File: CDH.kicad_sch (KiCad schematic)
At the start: 45 parts, among them J3 G125-MH12605M4P, J4 Conn_ARM_JTAG_SWD_10, U1 STM32H745BITx, U2 MCP2562FDT-H_SN

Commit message: PCB
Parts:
- C1, C10, C11, C12, C13, C14, C15, C16, C17, C18, C2, C21, C26, C27, C3, C4, C5, C6, C7, C8, C9: footprint (none) -> Capacitor_SMD:C_0402_1005Metric
- C19, C22, C23, C24, C28: footprint (none) -> Capacitor_SMD:C_0805_2012Metric
- C20: footprint (none) -> Capacitor_SMD:C_0603_1608Metric
- C25: value C -> 100n; footprint (none) -> Capacitor_SMD:C_0402_1005Metric
- FB1: footprint (none) -> Inductor_SMD:L_0201_0603Metric
- J4: footprint (none) -> Connector_PinHeader_1.27mm:PinHeader_2x05_P1.27mm_Horizontal
- JP1: footprint (none) -> Jumper:SolderJumper-2_P1.3mm_Bridged2Bar_Pad1.0x1.5mm
- JP2: footprint (none) -> Jumper:SolderJumper-2_P1.3mm_Open_Pad1.0x1.5mm
- PC104_H1, PC104_H2: footprint (none) -> Connector_PinHeader_1.00mm:PinHeader_2x26_P1.00mm_Vertical
- R1, R2, R3, R4, R5, R6, R8: footprint (none) -> Resistor_SMD:R_0603_1608Metric
- SW_Reset1: footprint (none) -> Button_Switch_SMD:SW_Push_1P1T-SH_NO_CK_KMR2xxG
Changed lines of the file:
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@@
 			)
 		)
-		(property "Footprint" ""
+		(property "Footprint" "Capacitor_SMD:C_0402_1005Metric"
 			(at 268.9352 34.29 0)
 			(effects
@@
 			)
 		)
-		(property "Value" "C"
+		(property "Value" "100n"
 			(at 247.904 82.55 90)
 			(effects
@@
 			)
 		)
-		(property "Footprint" ""
+		(property "Footprint" "Capacitor_SMD:C_0402_1005Metric"
 			(at 241.3 79.7052 0)
 			(effects
@@
 			)
 		)
-		(property "Footprint" ""
+		(property "Footprint" "Resistor_SMD:R_0603_1608Metric"
 			(at 450.342 236.22 90)
 			(effects
@@
 			)
 		)
-		(property "Footprint" ""
+		(property "Footprint" "Capacitor_SMD:C_0603_1608Metric"
 			(at 346.4052 55.88 0)
 			(effects
@@
 			)
 		)
-		(property "Footprint" ""
+		(property "Footprint" "Capacitor_SMD:C_0805_2012Metric"
 			(at 341.63 75.2348 0)
 			(effects
@@
 			)
 		)
-		(property "Footprint" ""
+		(property "Footprint" "Capacitor_SMD:C_0402_1005Metric"
 			(at 277.8252 34.29 0)
 			(effects
@@
 			)
 		)
-		(property "Footprint" ""
+		(property "Footprint" "Capacitor_SMD:C_0402_1005Metric"
 			(at 286.7152 55.88 0)
 			(effects
@@
 			)
 		)
-		(property "Footprint" ""
+		(property "Footprint" "Resistor_SMD:R_0603_1608Metric"
 			(at 239.522 270.51 90)
 			(effects
@@
 			)
 		)
-		(property "Footprint" ""
+		(property "Footprint" "Capacitor_SMD:C_0402_1005Metric"
 			(at 322.2752 55.88 0)
 			(effects
@@
 			)
 		)
-		(property "Footprint" ""
+		(property "Footprint" "Capacitor_SMD:C_0402_1005Metric"
 			(at 295.6052 34.29 0)
 			(effects
@@
 			)
 		)
-		(property "Footprint" ""
+		(property "Footprint" "Capacitor_SMD:C_0805_2012Metric"
 			(at 247.65 316.5348 0)
 			(effects
@@
 			)
 		)
-		(property "Footprint" ""
+		(property "Footprint" "Resistor_SMD:R_0603_1608Metric"
 			(at 239.522 260.35 90)
 			(effects
@@
 			)
 		)
-		(property "Footprint" ""
+		(property "Footprint" "Resistor_SMD:R_0603_1608Metric"
 			(at 367.792 153.67 90)
 			(effects
@@
 			)
 		)
-		(property "Footprint" ""
+		(property "Footprint" "Capacitor_SMD:C_0402_1005Metric"
 			(at 313.3852 34.29 0)
 			(effects
@@
 			)
 		)
-		(property "Footprint" ""
+		(property "Footprint" "Capacitor_SMD:C_0402_1005Metric"
 			(at 331.1652 34.29 0)
 			(effects
@@
 			)
 		)
-		(property "Footprint" ""
+		(property "Footprint" "Capacitor_SMD:C_0402_1005Metric"
 			(at 357.8352 55.88 0)
 			(effects
@@
 			)
 		)
-		(property "Footprint" ""
+		(property "Footprint" "Capacitor_SMD:C_0402_1005Metric"
 			(at 176.53 129.8448 0)
 			(effects
@@
 			)
 		)
-		(property "Footprint" ""
+		(property "Footprint" "Capacitor_SMD:C_0805_2012Metric"
 			(at 247.65 300.0248 0)
 			(effects
@@
 			)
 		)
-		(property "Footprint" ""
+		(property "Footprint" "Capacitor_SMD:C_0402_1005Metric"
 			(at 304.4952 34.29 0)
 			(effects
@@
 			)
 		)
-		(property "Footprint" ""
+		(property "Footprint" "Capacitor_SMD:C_0402_1005Metric"
 			(at 175.26 142.5448 0)
 			(effects
@@
 			)
 		)
-		(property "Footprint" ""
+		(property "Footprint" "Capacitor_SMD:C_0402_1005Metric"
 			(at 331.1652 55.88 0)
 			(effects
@@
 			)
 		)
-		(property "Footprint" ""
+		(property "Footprint" "Connector_PinHeader_1.00mm:PinHeader_2x26_P1.00mm_Vertical"
 			(at 416.56 144.78 0)
 			(effects
@@
 			)
 		)
-		(property "Footprint" ""
+		(property "Footprint" "Inductor_SMD:L_0201_0603Metric"
 			(at 288.29 66.548 90)
 			(effects
@@
 			)
 		)
-		(property "Footprint" ""
+		(property "Footprint" "Capacitor_SMD:C_0805_2012Metric"
 			(at 247.65 308.9148 0)
 			(effects
@@
 			)
 		)
-		(property "Footprint" ""
+		(property "Footprint" "Resistor_SMD:R_0603_1608Metric"
 			(at 371.348 143.51 90)
 			(effects
@@
 			)
 		)
-		(property "Footprint" ""
+		(property "Footprint" "Capacitor_SMD:C_0805_2012Metric"
 			(at 342.5952 34.29 0)
 			(effects
@@
 			)
 		)
-		(property "Footprint" ""
+		(property "Footprint" "Capacitor_SMD:C_0402_1005Metric"
 			(at 286.7152 34.29 0)
 			(effects
@@
 			)
 		)
-		(property "Footprint" ""
+		(property "Footprint" "Capacitor_SMD:C_0402_1005Metric"
 			(at 277.8252 55.88 0)
 			(effects
@@
 			)
 		)
-		(property "Footprint" ""
+		(property "Footprint" "Capacitor_SMD:C_0402_1005Metric"
 			(at 313.3852 55.88 0)
 			(effects
@@
 			)
 		)
-		(property "Footprint" ""
+		(property "Footprint" "Capacitor_SMD:C_0402_1005Metric"
 			(at 304.4952 55.88 0)
 			(effects
@@
 			)
 		)
-		(property "Footprint" ""
+		(property "Footprint" "Connector_PinHeader_1.00mm:PinHeader_2x26_P1.00mm_Vertical"
 			(at 445.77 144.78 0)
 			(effects
@@
 			)
 		)
-		(property "Footprint" ""
+		(property "Footprint" "Button_Switch_SMD:SW_Push_1P1T-SH_NO_CK_KMR2xxG"
 			(at 245.11 68.58 0)
 			(effects
@@
 			)
 		)
-		(property "Footprint" ""
+		(property "Footprint" "Connector_PinHeader_1.27mm:PinHeader_2x05_P1.27mm_Horizontal"
 			(at 434.34 247.65 0)
 			(effects
@@
 			)
 		)
-		(property "Footprint" ""
+		(property "Footprint" "Jumper:SolderJumper-2_P1.3mm_Bridged2Bar_Pad1.0x1.5mm"
 			(at 246.38 93.98 0)
 			(effects
@@
 			)
 		)
-		(property "Footprint" ""
+		(property "Footprint" "Resistor_SMD:R_0603_1608Metric"
 			(at 116.332 149.86 90)
 			(effects
@@
 			)
 		)
-		(property "Footprint" ""
+		(property "Footprint" "Jumper:SolderJumper-2_P1.3mm_Open_Pad1.0x1.5mm"
 			(at 118.11 139.7 0)
 			(effects
@@
 			)
 		)
-		(property "Footprint" ""
+		(property "Footprint" "Capacitor_SMD:C_0402_1005Metric"
 			(at 268.9352 55.88 0)
 			(effects
@@
 			)
 		)
-		(property "Footprint" ""
+		(property "Footprint" "Capacitor_SMD:C_0402_1005Metric"
 			(at 322.2752 34.29 0)
 			(effects
@@
 			)
 		)
-		(property "Footprint" ""
+		(property "Footprint" "Capacitor_SMD:C_0402_1005Metric"
 			(at 295.6052 55.88 0)
 			(effects
@@
 			)
 		)
-		(property "Footprint" ""
+		(property "Footprint" "Resistor_SMD:R_0603_1608Metric"
 			(at 238.76 90.678 90)
 			(effects
@@
 			)
 		)
-		(property "Footprint" ""
+		(property "Footprint" "Capacitor_SMD:C_0402_1005Metric"
 			(at 260.0452 34.29 0)
 			(effects
@@
 			)
 		)
-		(property "Footprint" ""
+		(property "Footprint" "Capacitor_SMD:C_0402_1005Metric"
 			(at 260.0452 55.88 0)
 			(effects

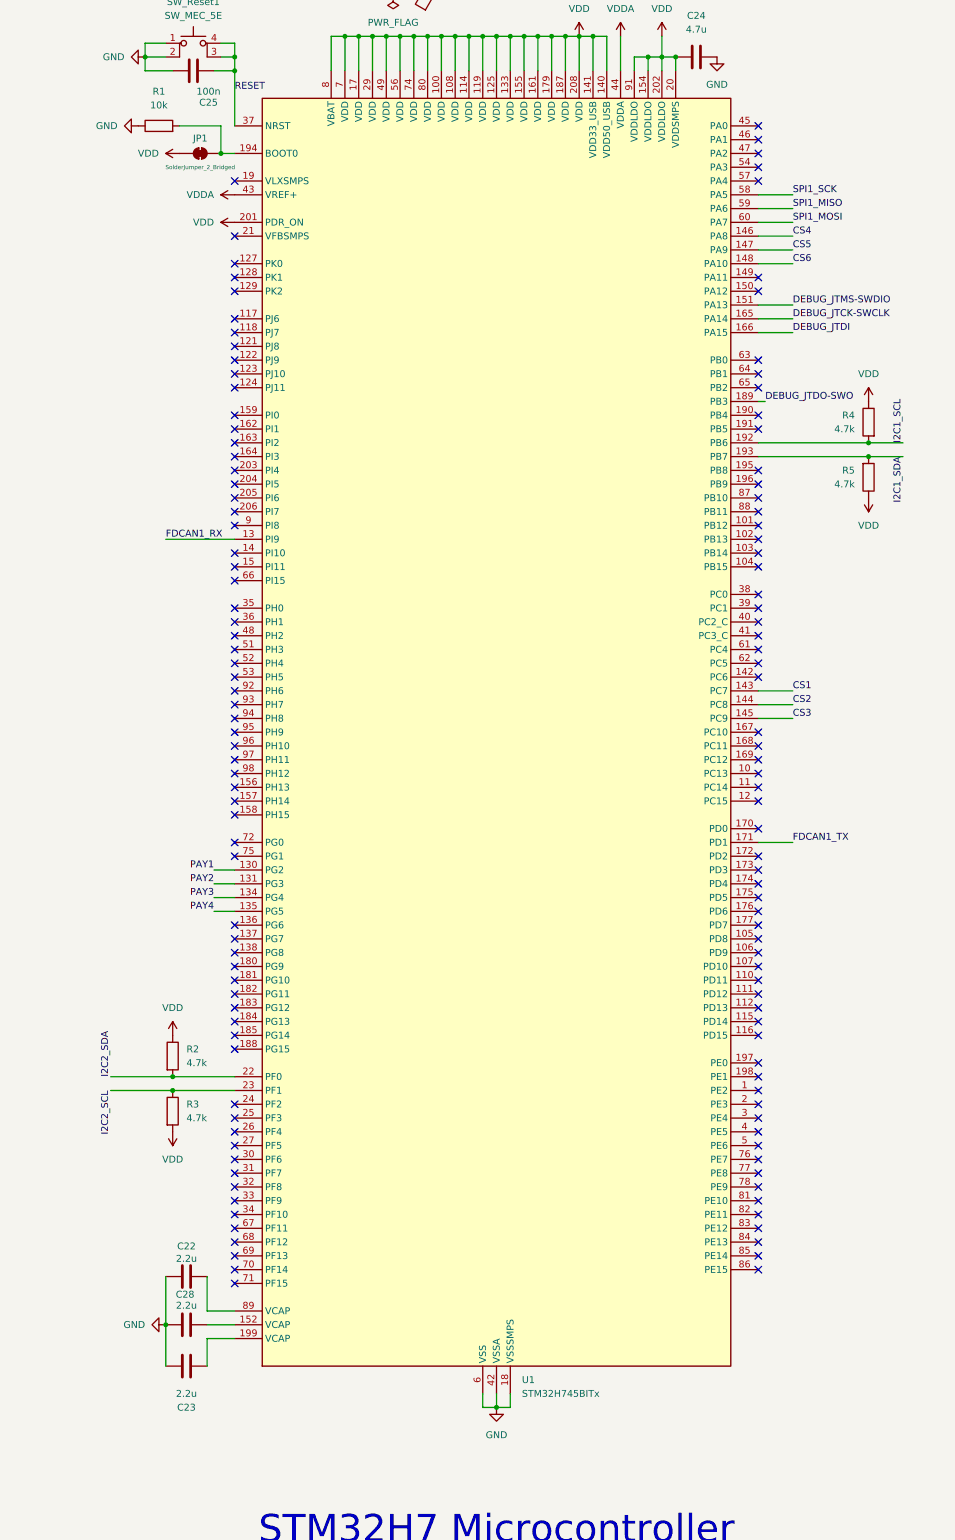
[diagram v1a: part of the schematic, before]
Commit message: changed STM32 symbol and made PCB 4 layers
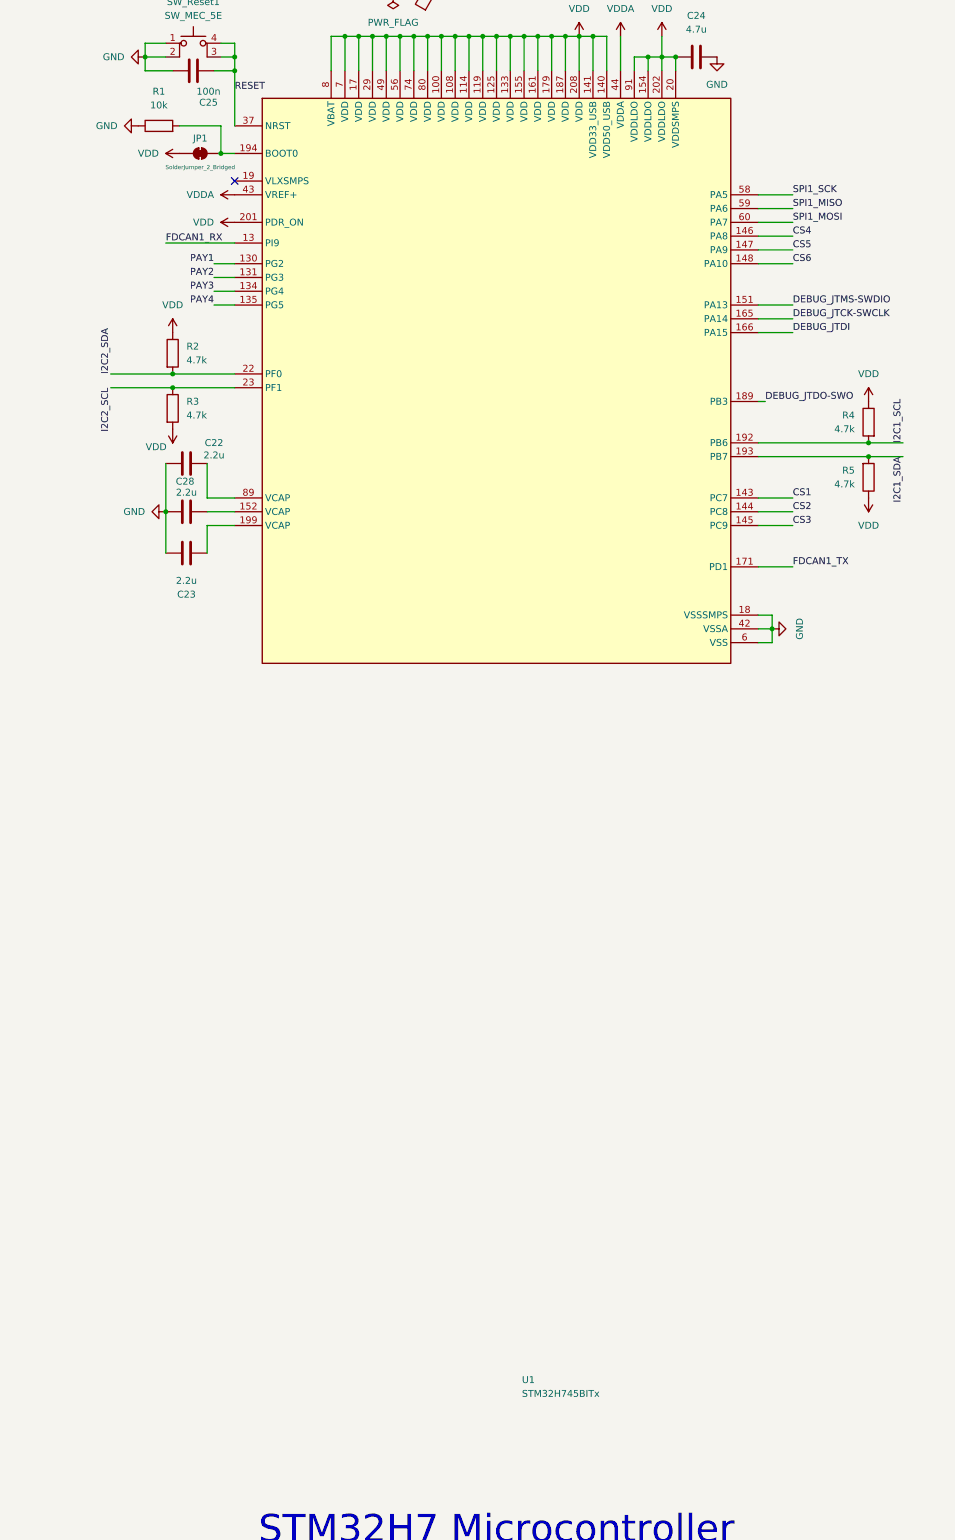
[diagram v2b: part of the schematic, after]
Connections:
- net CS1: now also U1.87 (PB10)
- net CS2: now also U1.88 (PB11)
- net CS3: now also U1.101 (PB12)
- net FDCAN1_TX: now also U1.104 (PB15)
- net GND: no longer U1.109 (VSS), U1.113 (VSS), U1.120 (VSS), U1.126 (VSS), U1.132 (VSS), U1.139 (VSS), U1.153 (VSS), U1.16 (VSS), U1.160 (VSS), U1.178 (VSS), U1.186 (VSS), U1.200 (VSS), U1.207 (VSS), U1.28 (VSS), U1.50 (VSS), U1.55 (VSS), U1.73 (VSS), U1.79 (VSS), U1.90 (VSS), U1.99 (VSS)
- net I2C2_SCL: now also U1.124 (PJ11)
- net I2C2_SDA: now also U1.123 (PJ10)
- net PAY1: now also U1.127 (PK0)
- net PAY2: now also U1.128 (PK1)
- net PAY3: now also U1.129 (PK2)
- net at C28.2, U1.152 (VCAP): now also U1.206 (PI7)
- net at C23.2, U1.199 (VCAP): now also U1.9 (PI8)
- net at U1.205 (PI6): now also C22.2, U1.89 (VCAP)
- new net: U1.109 (VSS), U1.113 (VSS), U1.120 (VSS), U1.126 (VSS), U1.132 (VSS), U1.139 (VSS), U1.153 (VSS), U1.16 (VSS), U1.160 (VSS), U1.178 (VSS), U1.186 (VSS), U1.200 (VSS), U1.207 (VSS), U1.28 (VSS), U1.50 (VSS), U1.55 (VSS), U1.73 (VSS), U1.79 (VSS), U1.90 (VSS), U1.99 (VSS)
- no-connect marks 224 -> 96
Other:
- moved on the sheet: C22, C23, C28, R2, R3
